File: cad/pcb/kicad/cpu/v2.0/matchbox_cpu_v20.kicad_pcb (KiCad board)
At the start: 6 copper layers, 40 x 66 mm, 64 parts, among them CN1 ?M02B-SRSS-TBS, P1 DF12-32-DP, P2 DF12-32-DP, P3 DF12-32-DP, P4 DF12-32-DP, Q1 FDN360P, Q2 FDN360P, SW1 B3U-3100PM-B, SW2 B3U-3100PM-B, U2 MCP1703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

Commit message: More CPU v20 changes
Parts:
- added C2: 0.1uF, matchbox_cpu_v20:0805, F.Cu at (120.0, 95.8)
- added C23: 1uF, matchbox_cpu_v20:0805, F.Cu at (122.6, 95.7)
- added C6: 1uF, matchbox_cpu_v20:0805, F.Cu at (125.4, 95.7)
- added J2: Conn_ARM_JTAG_SWD_10, Connector_Samtec:Samtec_LSHM-105-xx.x-x-DV-N_2x05_P0.50mm_Vertical, B.Cu at (121.7, 101.5)
- moved D5 21.6 mm to (147.9, 101.7), turned to 90 degrees
- moved R10 17.9 mm to (145.4, 101.6), turned to 270 degrees
- moved Q2 15.9 mm to (151.3, 101.7), turned to 270 degrees
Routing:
- net /VCC: track 92.9 -> 56.6 mm, vias 2 -> 0
- net /RESET#: track 40.6 -> 19.0 mm, vias 4 -> 2
- net /VCC_3V3: track 126.3 -> 104.8 mm
- net /VCC_USBF: track 45.8 -> 28.7 mm
- net /PWR_ON: track 82.1 -> 70.8 mm, vias 8 -> 5
- net /PB11: track 43.8 -> 33.3 mm
- net /USB_ID: track 59.6 -> 63.8 mm
- net /VBAT: track 28.8 -> 24.7 mm
- net /PB2: track 56.2 -> 52.5 mm
- net /USB_D-: track 68.4 -> 67.3 mm
- net /PA0: track 40.5 -> 39.7 mm
- net /PA3: track 41.8 -> 41.0 mm
- net /PA1: track 40.2 -> 39.5 mm
- net /PA2: track 41.4 -> 40.7 mm
- net /PB1: track 35.3 -> 34.6 mm
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
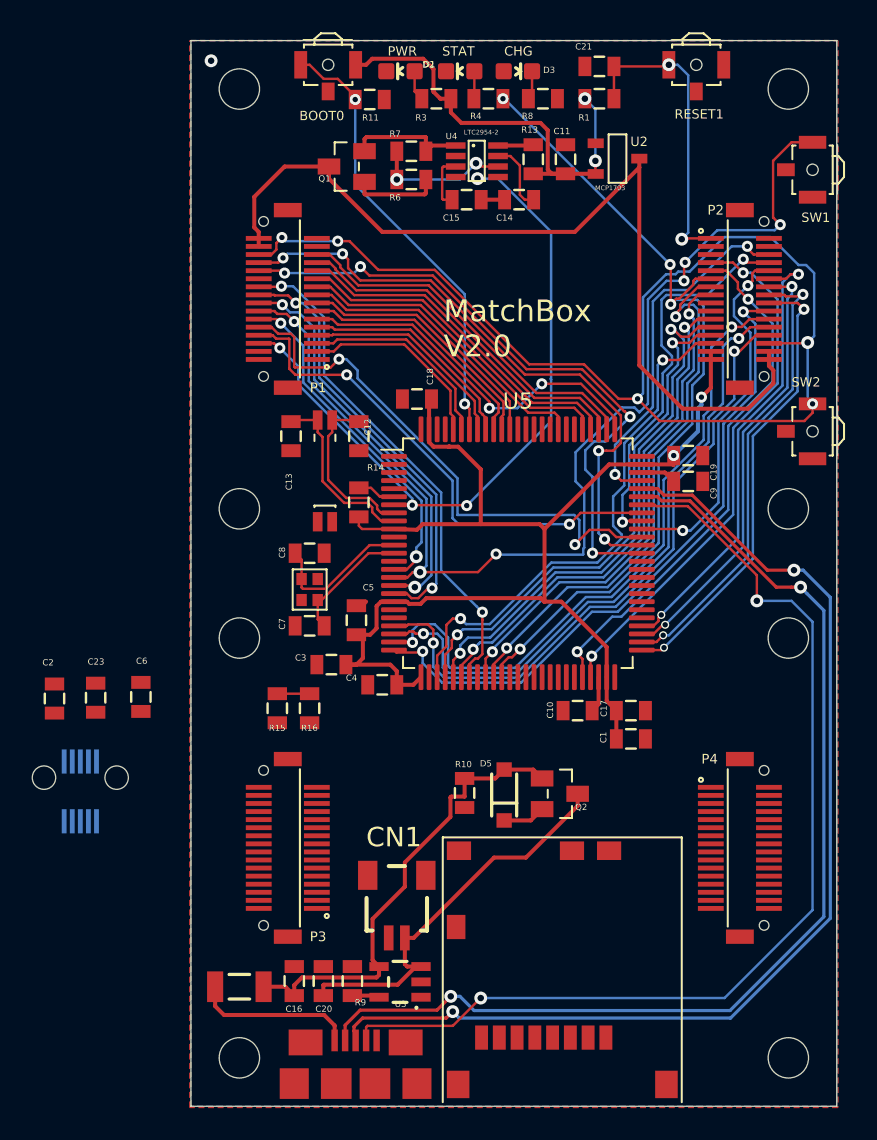
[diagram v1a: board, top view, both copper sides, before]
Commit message: Routed CPU v2.0. Needs cleanup.
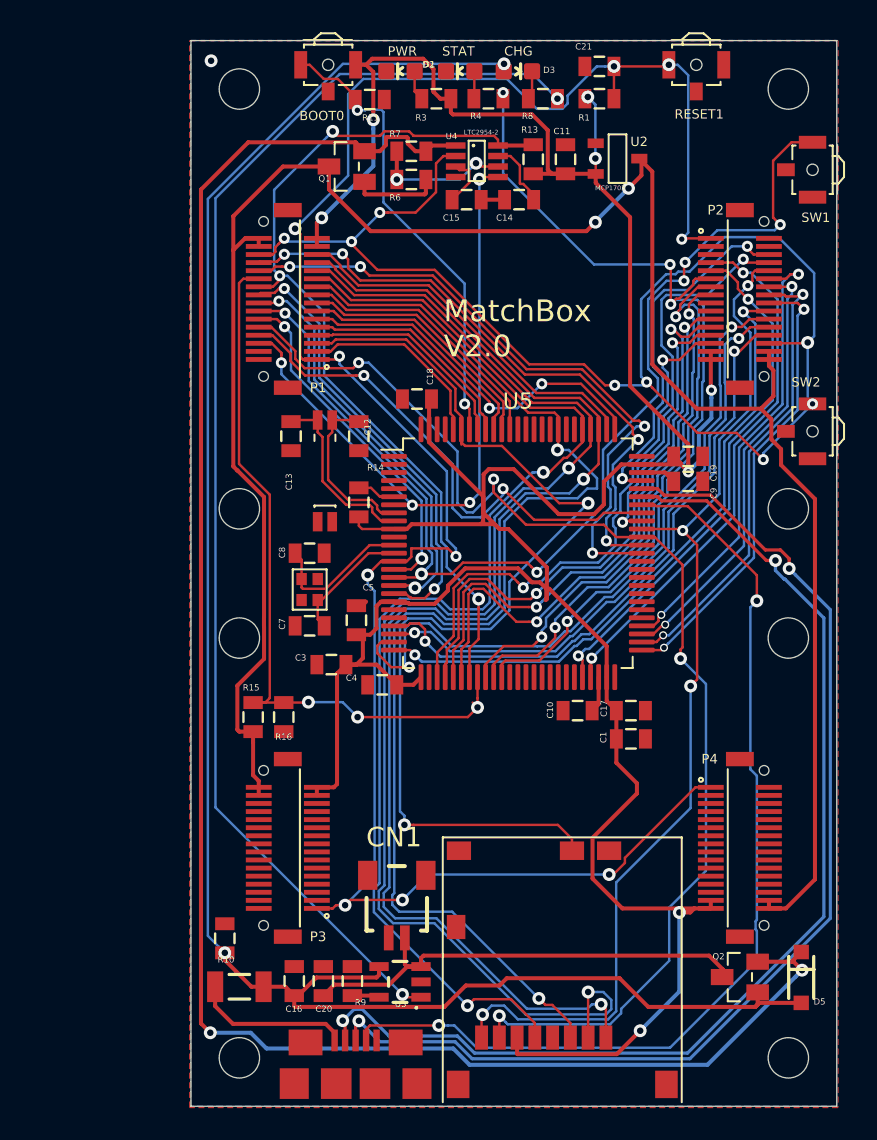
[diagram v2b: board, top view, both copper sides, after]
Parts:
- removed C2: 0.1uF, matchbox_cpu_v20:0805
- removed C23, C6: 1uF, matchbox_cpu_v20:0805
- removed J2: Conn_ARM_JTAG_SWD_10, Connector_Samtec:Samtec_LSHM-105-xx.x-x-DV-N_2x05_P0.50mm_Vertical
- moved D5 21.6 mm to (166.3, 113.0), turned to 270 degrees
- moved R10 17.4 mm to (130.6, 110.6), turned to 90 degrees
- moved Q2 15.9 mm to (162.5, 113.0), turned to 90 degrees
- moved R16 1.69 mm to (134.2, 96.9)
- moved R15 1.60 mm to (132.3, 96.9)
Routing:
- net /RESET#: track 19.0 -> 129.5 mm, vias 2 -> 10
- net /VCC_SEL: track 10.1 -> 114.7 mm, vias 0 -> 2
- net /VCC_3V3: track 104.8 -> 197.2 mm, vias 4 -> 8
- net /VCC_USBF: track 28.7 -> 116.0 mm, vias 0 -> 2
- net /STAT: track 0.00 -> 80.3 mm, vias 0 -> 2
- net /VCC: track 56.6 -> 131.7 mm, vias 0 -> 2
- net /PC11: track 21.5 -> 83.7 mm, vias 0 -> 2
- net /PC10: track 22.2 -> 81.2 mm, vias 0 -> 2
- net /PD2: track 19.1 -> 76.3 mm, vias 0 -> 2
- net /PC12: track 20.8 -> 74.7 mm, vias 0 -> 2
- net /PB8: track 12.6 -> 64.0 mm, vias 0 -> 2
- net /PC5: track 2.00 -> 45.8 mm, vias 0 -> 3
- net /PC8: track 34.3 -> 77.5 mm, vias 2 -> 4
- net /PC9: track 22.5 -> 65.0 mm, vias 2 -> 4
- net /PC4: track 33.9 -> 56.1 mm, vias 2 -> 3
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
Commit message: Lots of cleanup work on CPU v2
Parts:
- added C6: 1uF, matchbox_cpu_v20:0805, F.Cu at (160.2, 118.7)
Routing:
- net /VCC_3V3: track 197.2 -> 189.6 mm
- net /VCC_SEL: track 114.7 -> 119.1 mm
- net /STAT: track 80.3 -> 84.5 mm
- net /PC10: track 81.2 -> 77.4 mm
- net /PB8: track 64.0 -> 60.2 mm
- net /PA7: track 35.5 -> 31.7 mm
- net /PC11: track 83.7 -> 80.2 mm
- net /PD2: track 76.3 -> 73.2 mm
- net /PA6: track 36.2 -> 33.2 mm
- net /PA5: track 34.7 -> 31.9 mm
- net /PC4: track 56.1 -> 58.9 mm, vias 3 -> 5
- net /PC12: track 74.7 -> 72.0 mm
- net /PA4: track 34.2 -> 31.9 mm
- net /USB_D+: track 69.3 -> 67.3 mm
- net /PC8: track 77.5 -> 75.9 mm
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
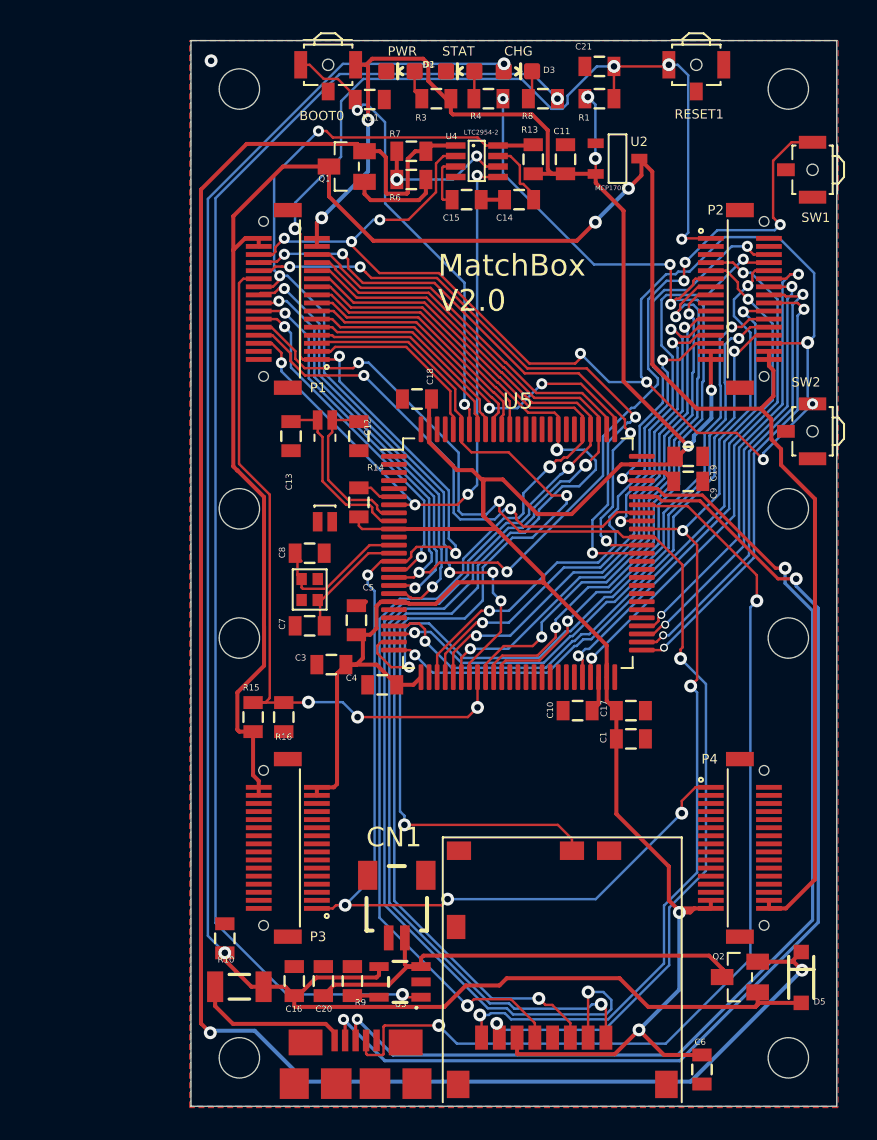
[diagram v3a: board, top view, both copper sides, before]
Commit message: Cleaned up decoupling caps and layout to maximize copper area.
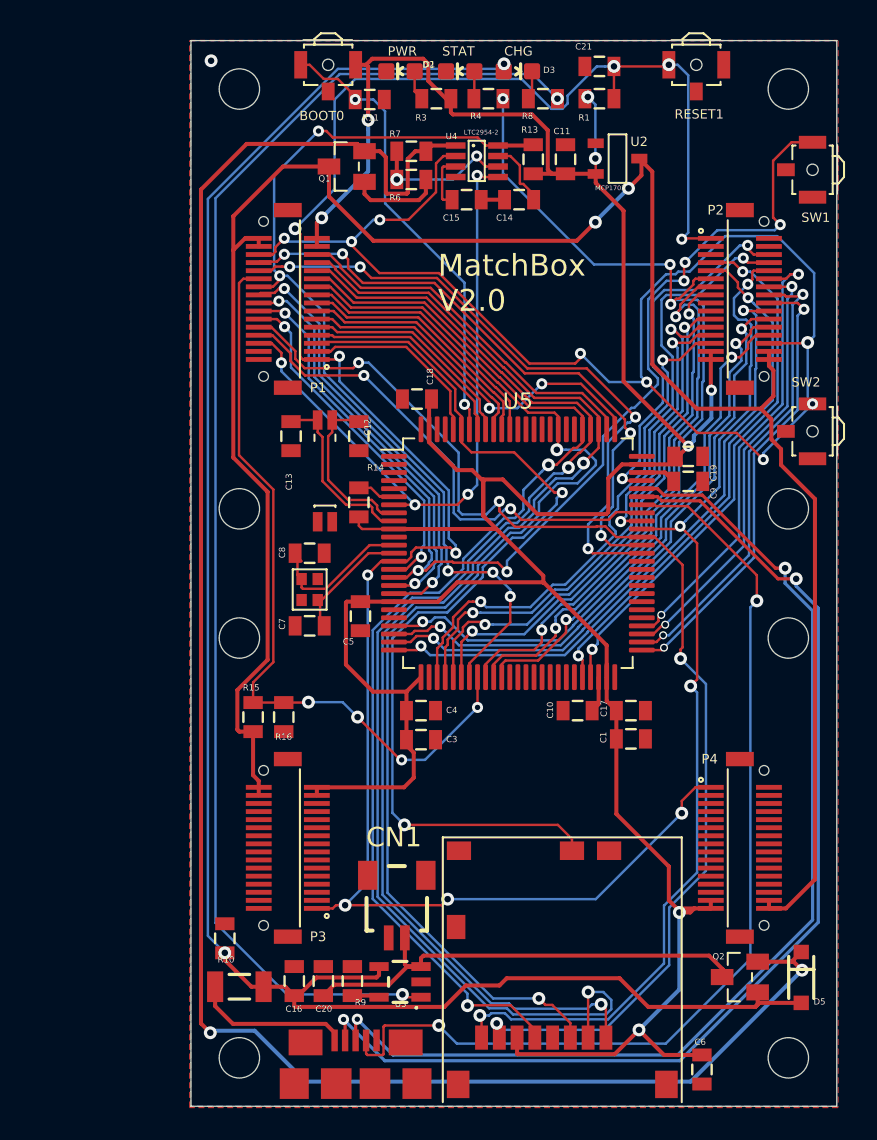
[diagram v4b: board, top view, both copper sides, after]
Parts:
- moved C3 7.24 mm to (142.8, 98.3), turned to 0 degrees
- moved C4 2.88 mm to (142.8, 96.5), turned to 0 degrees
- moved C5 0.35 mm to (139.0, 90.7), turned to 270 degrees
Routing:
- net /PA2: track 44.2 -> 37.7 mm
- net /VCC_3V3: track 189.6 -> 194.1 mm
- net /PA0: track 38.4 -> 36.1 mm
- net /PC5: track 45.4 -> 47.3 mm, vias 3 -> 4
- net /PB8: track 60.2 -> 59.0 mm
- net /PA1: track 38.1 -> 37.0 mm
- net /PA3: track 40.1 -> 39.4 mm
- net /PA4: track 31.9 -> 32.6 mm
- net /PA9: track 31.7 -> 31.2 mm
- net /PC12: track 72.0 -> 71.5 mm

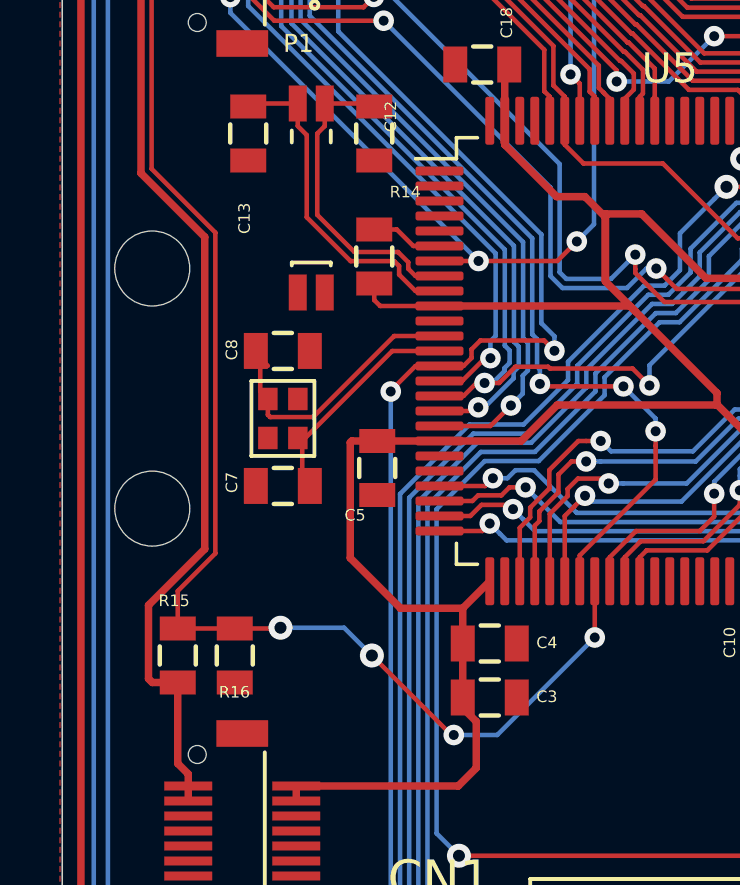
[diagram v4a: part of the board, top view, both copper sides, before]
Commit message: Basic CPU v2.0 with connections and some cleanup work.
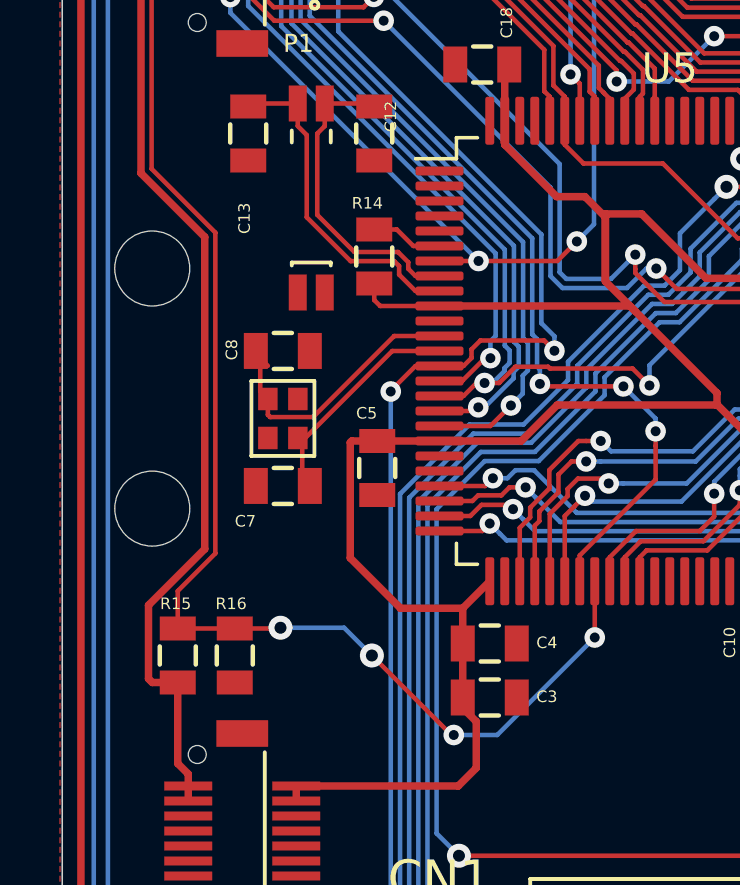
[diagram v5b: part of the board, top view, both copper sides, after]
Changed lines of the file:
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@@
   (module matchbox_cpu_v20:0805 (layer Top)
     (at 139 90.65 270)
-    (fp_text reference C5 (at 1.7995 0.387) (layer F.SilkS)
-      (effects (font (size 0.38608 0.38608) (thickness 0.030886)) (justify right bottom))
-    )
-    (fp_text value 0.1uF (at -1.428 0.841) (layer F.Fab)
+    (fp_text reference C5 (at -1.6 0) (layer F.SilkS)
+      (effects (font (size 0.38608 0.38608) (thickness 0.030886)) (justify right bottom))
+    )
+    (fp_text value 0.1uF (at 0.15 -0.8) (layer F.Fab)
       (effects (font (size 0.38608 0.38608) (thickness 0.030886)) (justify right bottom))
     )
@@
   (module matchbox_cpu_v20:ABM11 (layer Top)
     (at 135.8536 88.9989 270)
-    (fp_text reference Y1 (at -1.266 1.5 270) (layer F.Fab)
+    (fp_text reference Y1 (at -0.8489 2.0036 270) (layer F.Fab)
       (effects (font (size 0.7239 0.7239) (thickness 0.06096)) (justify right top))
     )
@@
   (module matchbox_cpu_v20:0805 (layer Top)
     (at 135.8536 91.2489 180)
-    (fp_text reference C7 (at 1.4755 -0.237 90) (layer F.SilkS)
-      (effects (font (size 0.38608 0.38608) (thickness 0.030886)) (justify left bottom))
-    )
-    (fp_text value 4pF (at -1.897 -0.316 90) (layer F.Fab)
+    (fp_text reference C7 (at 1.6036 -1.4011 180) (layer F.SilkS)
+      (effects (font (size 0.38608 0.38608) (thickness 0.030886)) (justify left bottom))
+    )
+    (fp_text value 4pF (at -0.3464 -1.3511 180) (layer F.Fab)
       (effects (font (size 0.38608 0.38608) (thickness 0.030886)) (justify left bottom))
     )
@@
   (module matchbox_cpu_v20:0805 (layer Top)
     (at 138.9 83.6 90)
-    (fp_text reference R14 (at 1.9245 0.512) (layer F.SilkS)
-      (effects (font (size 0.38608 0.38608) (thickness 0.030886)) (justify left bottom))
-    )
-    (fp_text value 0k (at -1.478 0.391) (layer F.Fab)
+    (fp_text reference R14 (at 1.55 -0.75) (layer F.SilkS)
+      (effects (font (size 0.38608 0.38608) (thickness 0.030886)) (justify left bottom))
+    )
+    (fp_text value 0k (at -0.25 -0.35) (layer F.Fab)
       (effects (font (size 0.38608 0.38608) (thickness 0.030886)) (justify left bottom))
     )
@@
   (module matchbox_cpu_v20:0805 (layer Top)
     (at 132.35 96.9 90)
-    (fp_text reference R15 (at 1.6 0.4) (layer F.SilkS)
-      (effects (font (size 0.38608 0.38608) (thickness 0.030886)) (justify right bottom))
-    )
-    (fp_text value 10k (at 0.75 -0.85) (layer F.Fab)
+    (fp_text reference R15 (at 1.5 0.45) (layer F.SilkS)
+      (effects (font (size 0.38608 0.38608) (thickness 0.030886)) (justify right bottom))
+    )
+    (fp_text value 10k (at -0.2 0.4) (layer F.Fab)
       (effects (font (size 0.38608 0.38608) (thickness 0.030886)) (justify right bottom))
     )
@@
   (module matchbox_cpu_v20:0805 (layer Top)
     (at 134.25 96.9 270)
-    (fp_text reference R16 (at 1.4505 -0.512) (layer F.SilkS)
-      (effects (font (size 0.38608 0.38608) (thickness 0.030886)) (justify right bottom))
-    )
-    (fp_text value 10k (at -2 -0.5) (layer F.Fab)
-      (effects (font (size 0.38608 0.38608) (thickness 0.030886)) (justify right bottom))
-    )
+    (fp_text reference R16 (at -1.5 -0.4) (layer F.SilkS)
+      (effects (font (size 0.38608 0.38608) (thickness 0.030886)) (justify right bottom))
+    )
+    (fp_text value 10k (at 0.15 -0.5) (layer F.Fab)
+      (effects (font (size 0.38608 0.38608) (thickness 0.030886)) (justify right bottom))
+    )

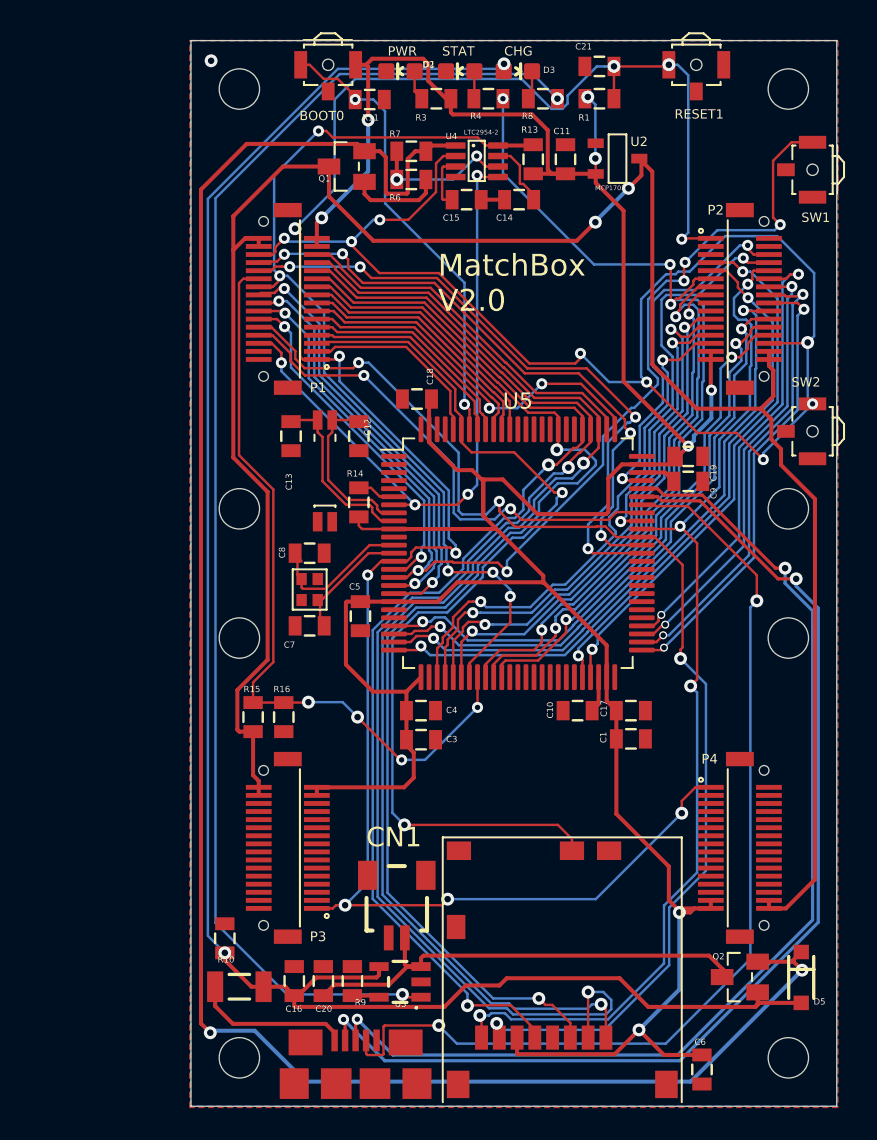
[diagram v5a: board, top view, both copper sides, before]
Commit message: Remove unnecessary RESET# pin pullup
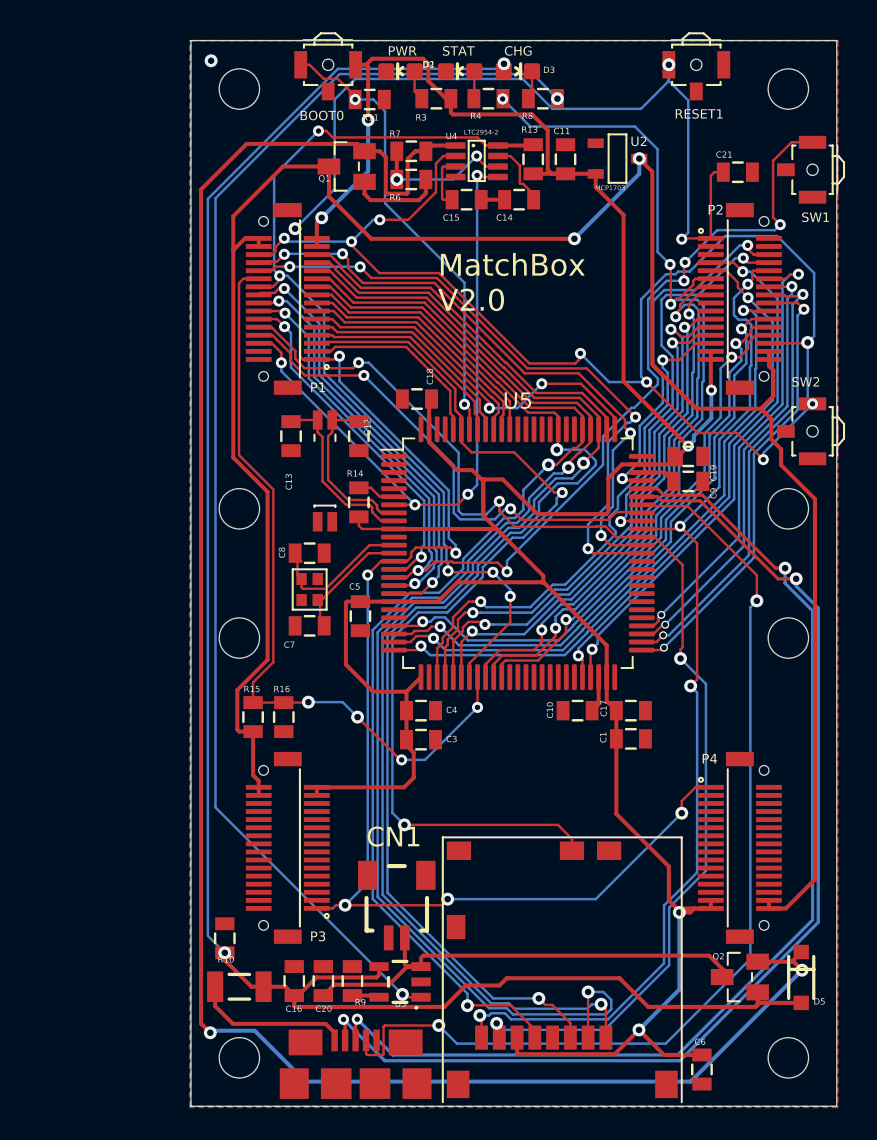
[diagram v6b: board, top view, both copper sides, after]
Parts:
- removed R1: 10k, matchbox_cpu_v20:0805
- moved C21 10.8 mm to (162.4, 63.1), turned to 0 degrees
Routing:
- net /VCC_3V3: track 194.1 -> 189.0 mm, vias 8 -> 6
- net /STAT: track 84.5 -> 80.3 mm
- net /RESET#: track 129.3 -> 132.2 mm, vias 10 -> 9
- net /PB2: track 55.3 -> 56.3 mm
